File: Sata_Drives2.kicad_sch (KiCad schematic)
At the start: 66 parts

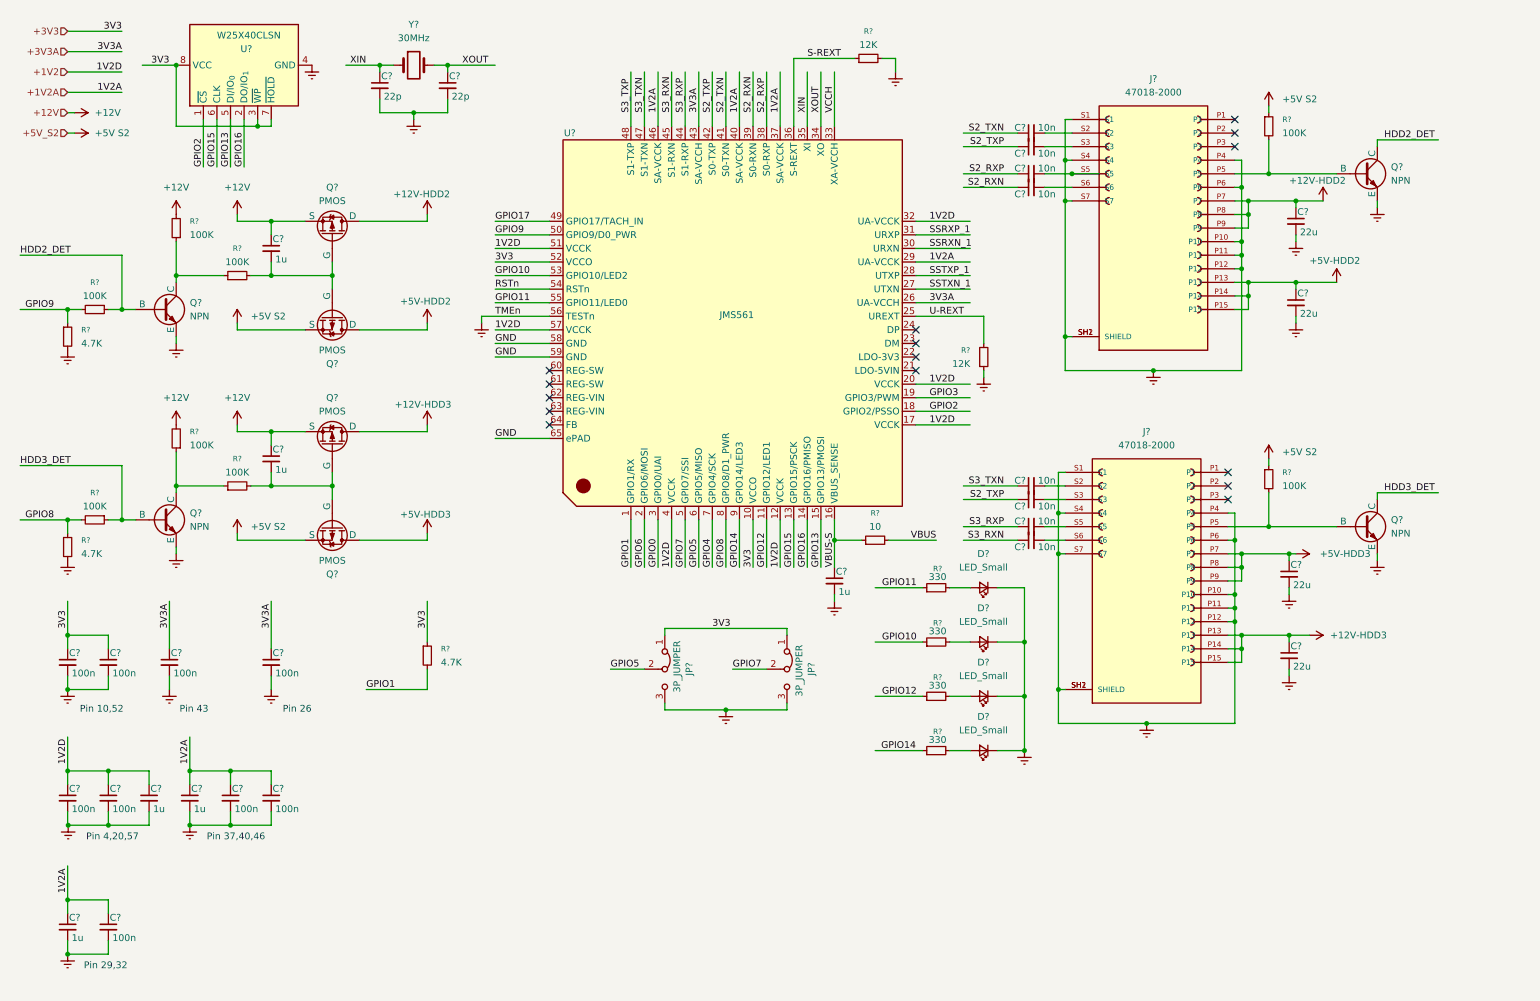
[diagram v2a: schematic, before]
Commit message: Sheets neatened
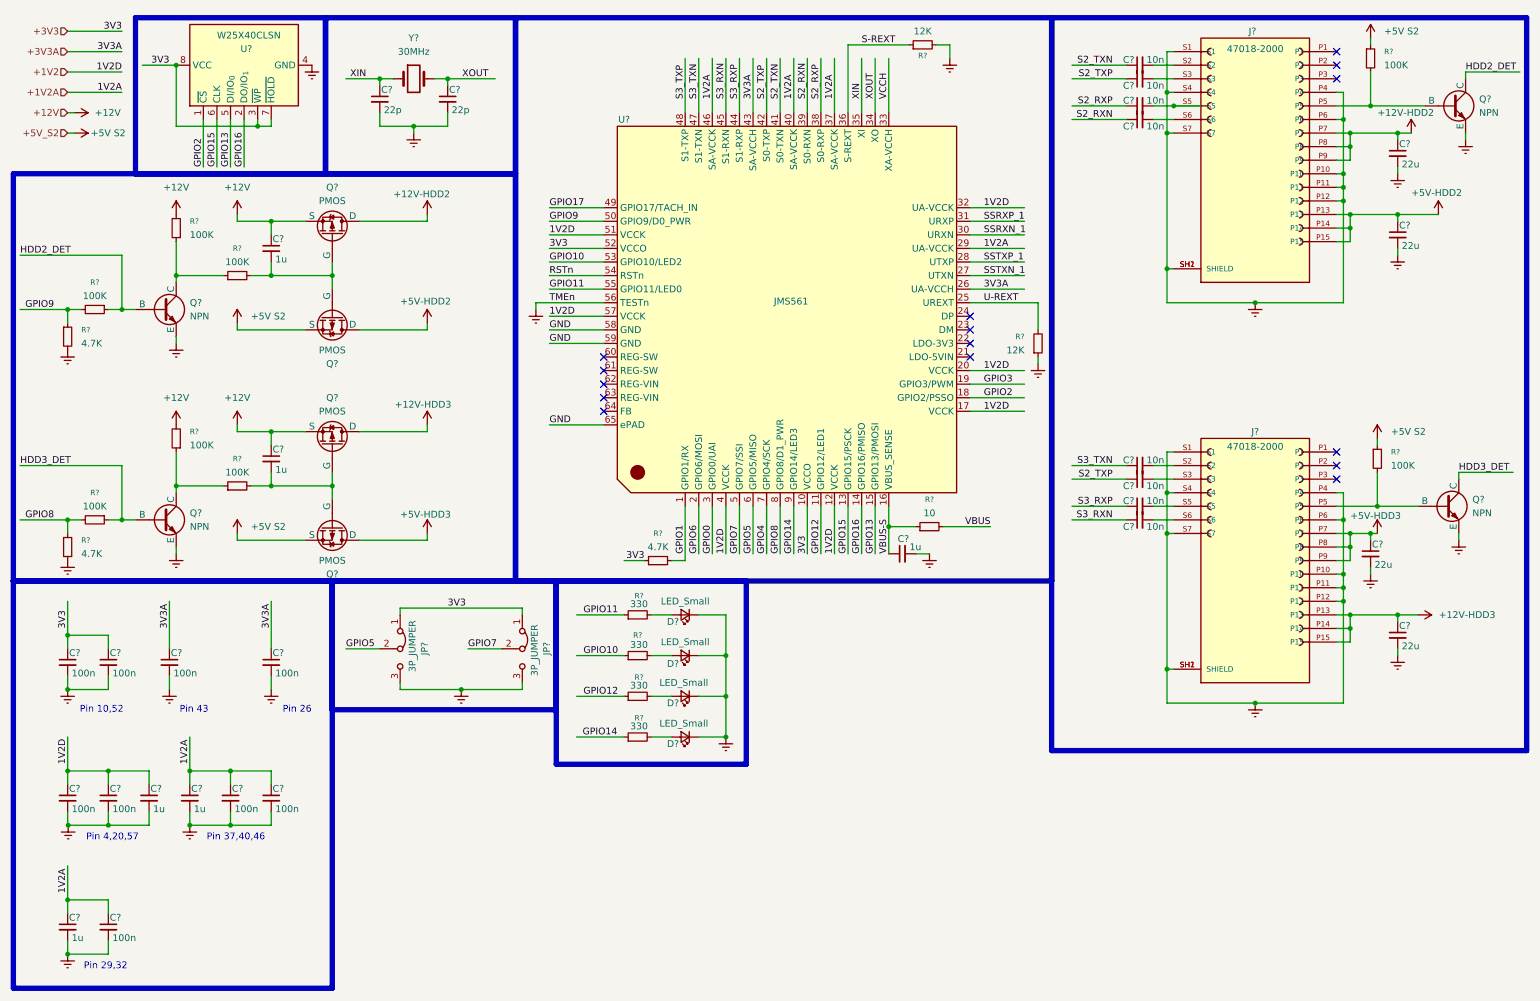
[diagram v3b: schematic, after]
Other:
- moved on the sheet: C?, D?, J?, JP?, Q?, R?, U?, Y?

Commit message: More Fans
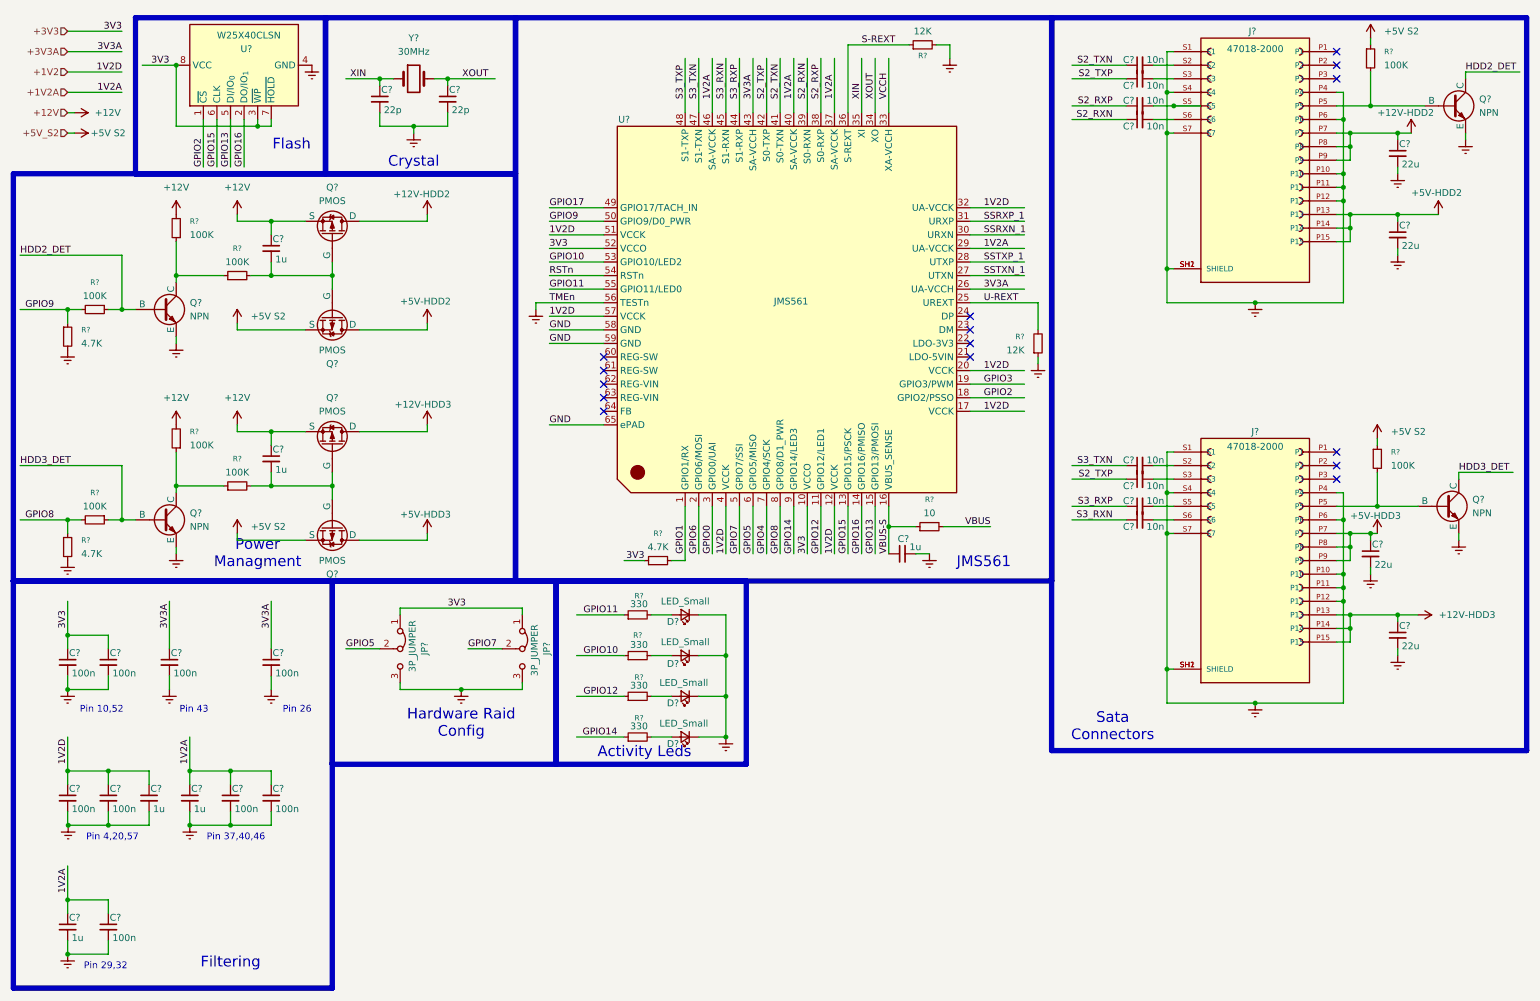
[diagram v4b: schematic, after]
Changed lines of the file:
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@@
 	(rectangle
 		(start 72.39 119.38)
-		(end 114.3 143.51)
+		(end 114.3 153.67)
 		(stroke
 			(width 1)
@@
 		)
 	)
+	(text_box "Crystal\n"
+		(exclude_from_sim no)
+		(at 73.66 34.29 0)
+		(size 27.94 9.525)
+		(margins 1.9049 1.9049 1.9049 1.9049)
+		(stroke
+			(width -0.0001)
+			(type solid)
+		)
+		(fill
+			(type none)
+		)
+		(effects
+			(font
+				(face "Times New Roman")
+				(size 2 2)
+				(thickness 0.3175)
+				(color 162 22 34 1)
+			)
+			(justify bottom)
+		)
+	)
+	(text_box "JMS561"
+		(exclude_from_sim no)
+		(at 180.34 109.22 0)
+		(size 27.94 9.525)
+		(margins 1.9049 1.9049 1.9049 1.9049)
+		(stroke
+			(width -0.0001)
+			(type solid)
+		)
+		(fill
+			(type none)
+		)
+		(effects
+			(font
+				(face "Times New Roman")
+				(size 2 2)
+				(thickness 0.3175)
+				(color 162 22 34 1)
+			)
+			(justify bottom)
+		)
+	)
+	(text_box "Flash\n\n"
+		(exclude_from_sim no)
+		(at 50.8 34.29 0)
+		(size 27.94 9.525)
+		(margins 1.9049 1.9049 1.9049 1.9049)
+		(stroke
+			(width -0.0001)
+			(type solid)
+		)
+		(fill
+			(type none)
+		)
+		(effects
+			(font
+				(face "Times New Roman")
+				(size 2 2)
+				(thickness 0.3175)
+				(color 162 22 34 1)
+			)
+			(justify bottom)
+		)
+	)
+	(text_box "Sata Connectors\n"
+		(exclude_from_sim no)
+		(at 204.47 141.605 0)
+		(size 27.94 9.525)
+		(margins 1.9049 1.9049 1.9049 1.9049)
+		(stroke
+			(width -0.0001)
+			(type solid)
+		)
+		(fill
+			(type none)
+		)
+		(effects
+			(font
+				(face "Times New Roman")
+				(size 2 2)
+				(thickness 0.3175)
+				(color 162 22 34 1)
+			)
+			(justify bottom)
+		)
+	)
+	(text_box "Power Managment\n"
+		(exclude_from_sim no)
+		(at 44.45 109.22 0)
+		(size 27.94 9.525)
+		(margins 1.9049 1.9049 1.9049 1.9049)
+		(stroke
+			(width -0.0001)
+			(type solid)
+		)
+		(fill
+			(type none)
+		)
+		(effects
+			(font
+				(face "Times New Roman")
+				(size 2 2)
+				(thickness 0.3175)
+				(color 162 22 34 1)
+			)
+			(justify bottom)
+		)
+	)
+	(text_box "Hardware Raid \nConfig\n"
+		(exclude_from_sim no)
+		(at 82.55 140.97 0)
+		(size 27.94 9.525)
+		(margins 1.9049 1.9049 1.9049 1.9049)
+		(stroke
+			(width -0.0001)
+			(type solid)
+		)
+		(fill
+			(type none)
+		)
+		(effects
+			(font
+				(face "Times New Roman")
+				(size 2 2)
+				(thickness 0.3175)
+				(color 162 22 34 1)
+			)
+			(justify bottom)
+		)
+	)
+	(text_box "Filtering"
+		(exclude_from_sim no)
+		(at 39.37 184.15 0)
+		(size 27.94 9.525)
+		(margins 1.9049 1.9049 1.9049 1.9049)
+		(stroke
+			(width -0.0001)
+			(type solid)
+		)
+		(fill
+			(type none)
+		)
+		(effects
+			(font
+				(face "Times New Roman")
+				(size 2 2)
+				(thickness 0.3175)
+				(color 162 22 34 1)
+			)
+			(justify bottom)
+		)
+	)
+	(text_box "Activity Leds\n"
+		(exclude_from_sim no)
+		(at 116.84 144.78 0)
+		(size 27.94 9.525)
+		(margins 1.9049 1.9049 1.9049 1.9049)
+		(stroke
+			(width -0.0001)
+			(type solid)
+		)
+		(fill
+			(type none)
+		)
+		(effects
+			(font
+				(face "Times New Roman")
+				(size 2 2)
+				(thickness 0.3175)
+				(color 162 22 34 1)
+			)
+			(justify bottom)
+		)
+	)
